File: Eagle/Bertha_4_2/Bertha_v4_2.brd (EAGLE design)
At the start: 100 x 84.6 mm, 124 parts, among them CON1 JACK_DC_BARREL, IC1 MCP1703DB, IC3 SN74LVC2G14, J1 RJ12RIGHTANGLE-I2C, J2 RJ12RIGHTANGLE-I2C, J7 22--02, Q1 BSP75, Q2 BSP75, Q3 BSP75, Q4 BSP75, Q5 BSP75, Q6 BSP75, U1 HX711, U100 RN2483, X2 16MHz, X3 FH12-08S-1SH, X4 MINI-USB

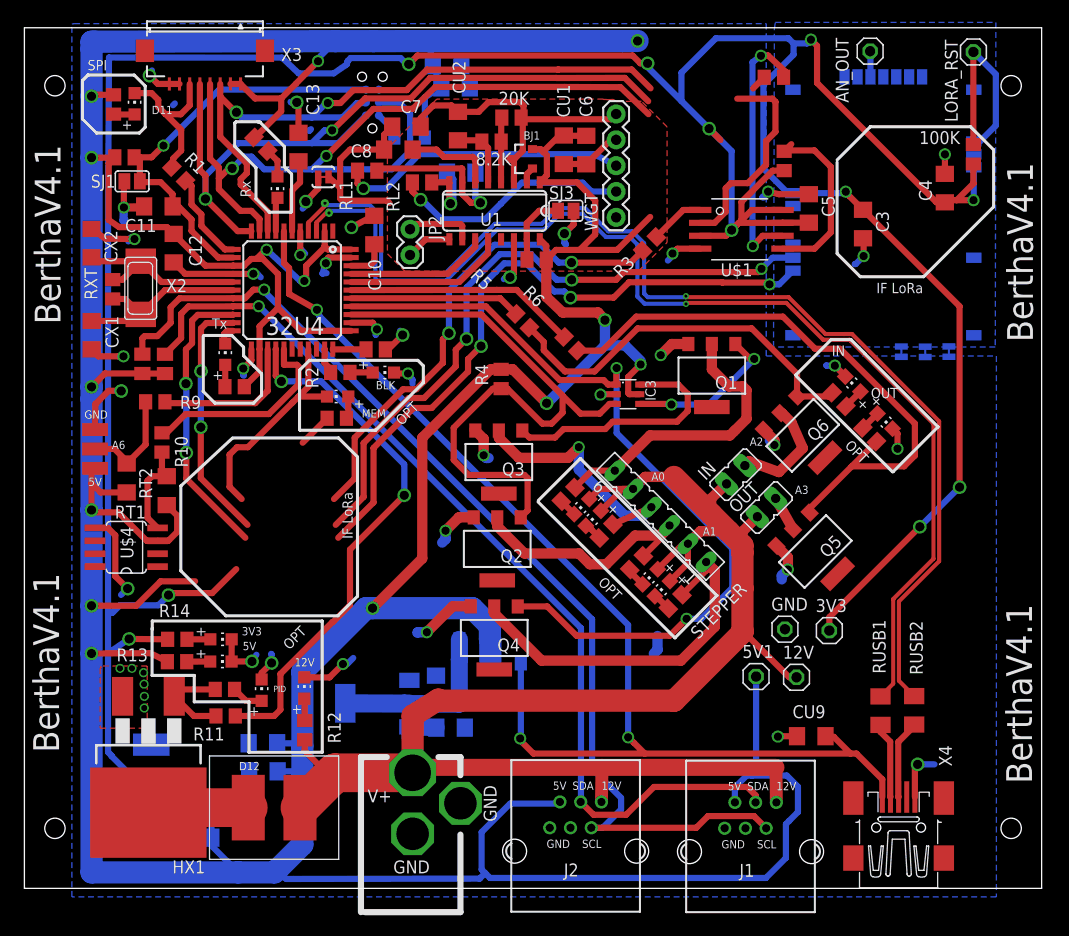
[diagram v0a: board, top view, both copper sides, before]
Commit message: bioreactor v4.2 revision, Lora Reset pin on D5, operation at 8MHz, 3.3V. The Flex cable is now exporting 12V instead of 5V (careful, not compatible with LCD V0.2 sudo git add --all), I2C ports are only providing 12V
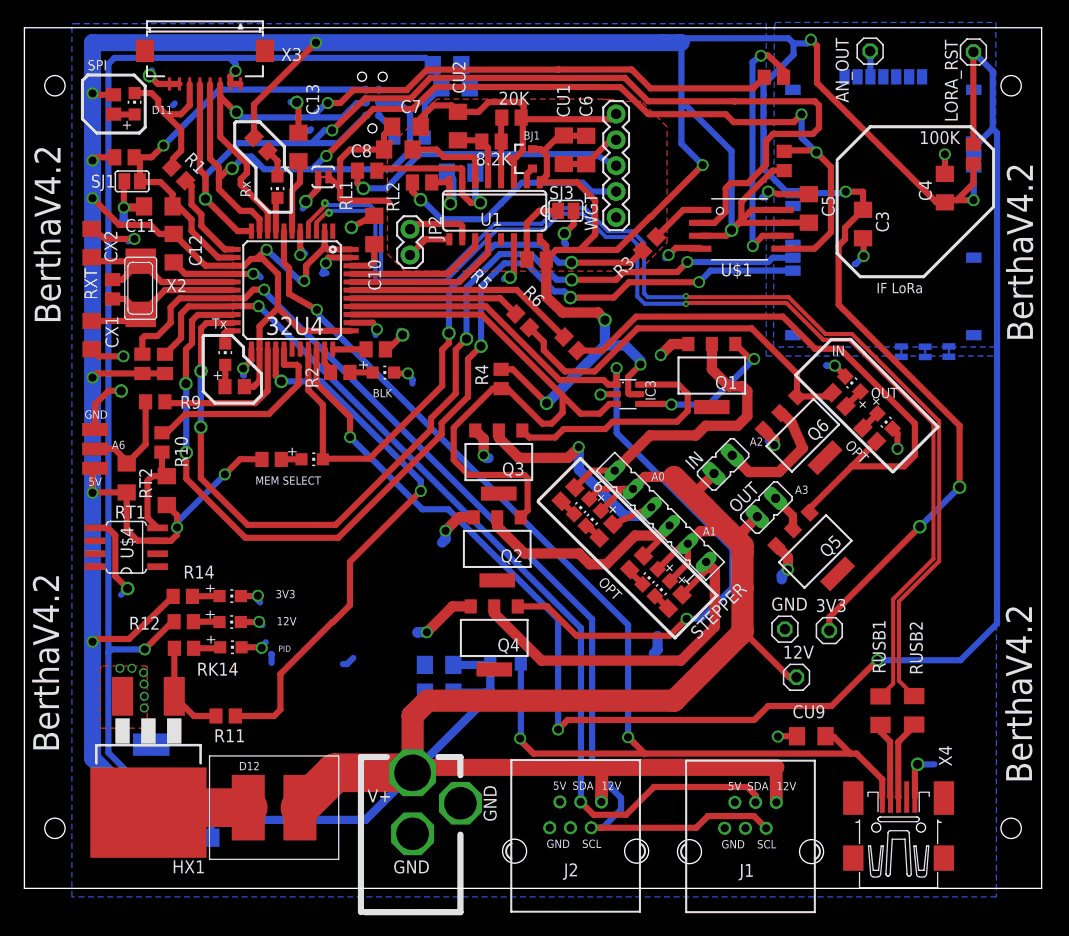
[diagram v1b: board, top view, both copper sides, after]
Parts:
- removed 5V1: (no value), Headerlibrary:1X01
- removed CU5, CU6: 10uF, rcl:C1206
- removed D3: 1N581D1206, lpatiny:LED-1206
- removed LDPW5: RED, adafruit:CHIP-LED0805
- removed R13: 1k, resistor:R0805
- removed U$2: NCP1117LPST50T3G, lpatiny:SOT223
- moved C2 19.0 mm to (35.8, 19.1)
- moved CU4 18.9 mm to (35.8, 16.3)
- moved R12 16.0 mm to (10.7, 23.3), turned to 180 degrees
- moved LDPW12 9.76 mm to (15.2, 23.3), turned to 270 degrees
- moved RK19 7.58 mm to (19.3, 39.3)
- moved LDMEM 6.66 mm to (23.3, 39.3), turned to 270 degrees
- moved RK14 5.70 mm to (10.7, 20.7)
- moved LDPID 5.19 mm to (15.3, 20.8), turned to 270 degrees
- moved LDPW3 4.34 mm to (15.2, 25.8)
- moved R14 4.25 mm to (10.6, 25.8)
- moved IN 1.60 mm to (63.7, 38.8)
- moved CU8 0.59 mm to (5.89, 2.12)
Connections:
- removed net +5V: CU5.1, D3.A, U$2.2, U$2.4
- removed net +5V/1: 32U4.14, 32U4.2, 32U4.24, 32U4.34, 32U4.44, 5V1.1, BJ1.2, C1.1, C12.2, C2.1, C6.1, CU1.1, CU3.1, CU4.1, CU7.1, D2.C, D3.C, D4.C, IC1.1, IC3.5, J1.+5V, J2.+5V, R13.1, R4.2, RK1.1, RK15.1, RK16.1, RK18.1, RK19.1, RK2.1, RK5.2, RK6.2, RT1.1, RT2.1, U$4.3, U$8.PIN3, U1.1, U1.16, X3.1, X3.2
- removed net LORA_RST: 100K.2, LORA_RST.1, U100.P$32
- removed net N$12: LDPW5.A, R13.2
- removed net RX3: U100.P$6
- removed net TX3: U100.P$7
- new net 5: J1.+5V, J2.+5V
- net +12V: now also C1.1, C2.1, CU3.1, CU4.1, CU7.1, D2.C, D4.C, IC1.1, X3.1, X3.2; no longer CU6.1, U$2.3
- net 3.3V: now also 32U4.14, 32U4.2, 32U4.24, 32U4.34, 32U4.44, BJ1.2, C12.2, C6.1, CU1.1, IC3.5, R4.2, RK1.1, RK15.1, RK16.1, RK18.1, RK19.1, RK2.1, RK5.2, RK6.2, RT1.1, RT2.1, U$4.3, U$8.PIN3, U1.1, U1.16
- net D5*: now also 100K.2, LORA_RST.1, U100.P$32
- net GND: no longer CU5.2, CU6.2, LDPW5.C, U$2.1
- net RX: now also U100.P$6
- net TX: now also U100.P$7
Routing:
- net +5V/1: track 555.3 -> 0.00 mm, vias 14 -> 0
- net 3.3V: track 325.1 -> 516.1 mm, vias 11 -> 21
- net +12V: track 169.0 -> 334.8 mm, vias 0 -> 2
- net D5*: track 0.00 -> 164.8 mm, vias 0 -> 3
- net RX: track 28.3 -> 102.0 mm, vias 2 -> 5
- net TX: track 24.6 -> 97.3 mm, vias 2 -> 5
- net RX3: track 65.8 -> 0.00 mm, vias 3 -> 0
- net TX3: track 64.9 -> 0.00 mm, vias 3 -> 0
- net LORA_RST: track 20.1 -> 0.00 mm
- net MOSI: track 100.9 -> 119.9 mm, vias 2 -> 4
- net +5V: track 18.6 -> 0.00 mm
- net MISO: track 95.2 -> 112.0 mm
- net D10*: track 69.9 -> 57.9 mm
- net SCK: track 70.3 -> 80.3 mm
- net GND: track 151.4 -> 148.1 mm
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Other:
- board text added: "BerthaV4.2"
- board text added: "MEM SELECT"
- board text removed: "BerthaV4.1"
- board text removed: "MEM"
- board text removed: "No LoRa"
